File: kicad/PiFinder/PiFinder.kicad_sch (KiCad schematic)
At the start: 24 parts, among them J1 Raspberry_Pi_2_3, J2 display, J3 IMU, SW0 SW_Push_Dual, SW1 SW_Push_Dual, SW2 SW_Push_Dual, SW3 SW_Push_Dual, SW4 SW_Push_Dual, SW5 SW_Push_Dual, SW6 SW_Push_Dual, SW7 SW_Push_Dual, SW8 SW_Push_Dual, SW9 SW_Push_Dual

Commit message: Working capture/solver
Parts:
- J2: symbol Connector:Conn_01x08_Male -> Connector:Conn_01x07_Male
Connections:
- net DISP_CLK: now also J2.4 (Pin_4); no longer J2.5 (Pin_5)
- net DISP_CS: now also J2.5 (Pin_5); no longer J2.6 (Pin_6)
- net DISP_DC: now also J2.6 (Pin_6); no longer J2.7 (Pin_7)
- net DISP_DIN: now also J2.3 (Pin_3); no longer J2.4 (Pin_4)
- net DISP_RST: now also J2.7 (Pin_7); no longer J2.8 (Pin_8)
- no-connect marks 3 -> 2
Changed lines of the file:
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@@
   (junction (at 46.99 180.34) (diameter 0) (color 0 0 0 0)
   )
-  (no_connect (at 45.72 43.18))
   (no_connect (at 99.06 53.34))
   (no_connect (at 99.06 43.18))
@@
     )
   )
-  (global_label "DISP_DC" (shape input) (at 45.72 53.34 0) (fields_autoplaced)
-    (effects (font (size 1.27 1.27)) (justify left))
-    (property "Intersheet References" "${INTERSHEET_REFS}" (id 0) (at 55.9061 53.2606 0)
+  (global_label "DISP_DC" (shape input) (at 45.72 50.8 0) (fields_autoplaced)
+    (effects (font (size 1.27 1.27)) (justify left))
+    (property "Intersheet References" "${INTERSHEET_REFS}" (id 0) (at 55.9061 50.7206 0)
       (effects (font (size 1.27 1.27)) (justify left) hide)
     )
@@
     )
   )
-  (global_label "DISP_RST" (shape input) (at 45.72 55.88 0) (fields_autoplaced)
-    (effects (font (size 1.27 1.27)) (justify left))
-    (property "Intersheet References" "${INTERSHEET_REFS}" (id 0) (at 56.8132 55.8006 0)
-      (effects (font (size 1.27 1.27)) (justify left) hide)
-    )
-  )
-  (global_label "DISP_CLK" (shape input) (at 45.72 48.26 0) (fields_autoplaced)
-    (effects (font (size 1.27 1.27)) (justify left))
-    (property "Intersheet References" "${INTERSHEET_REFS}" (id 0) (at 56.9342 48.1806 0)
-      (effects (font (size 1.27 1.27)) (justify left) hide)
-    )
-  )
-  (global_label "DISP_CS" (shape input) (at 45.72 50.8 0) (fields_autoplaced)
-    (effects (font (size 1.27 1.27)) (justify left))
-    (property "Intersheet References" "${INTERSHEET_REFS}" (id 0) (at 55.8456 50.7206 0)
+  (global_label "DISP_RST" (shape input) (at 45.72 53.34 0) (fields_autoplaced)
+    (effects (font (size 1.27 1.27)) (justify left))
+    (property "Intersheet References" "${INTERSHEET_REFS}" (id 0) (at 56.8132 53.2606 0)
+      (effects (font (size 1.27 1.27)) (justify left) hide)
+    )
+  )
+  (global_label "DISP_CLK" (shape input) (at 45.72 45.72 0) (fields_autoplaced)
+    (effects (font (size 1.27 1.27)) (justify left))
+    (property "Intersheet References" "${INTERSHEET_REFS}" (id 0) (at 56.9342 45.6406 0)
+      (effects (font (size 1.27 1.27)) (justify left) hide)
+    )
+  )
+  (global_label "DISP_CS" (shape input) (at 45.72 48.26 0) (fields_autoplaced)
+    (effects (font (size 1.27 1.27)) (justify left))
+    (property "Intersheet References" "${INTERSHEET_REFS}" (id 0) (at 55.8456 48.1806 0)
       (effects (font (size 1.27 1.27)) (justify left) hide)
     )
@@
     )
   )
-  (global_label "DISP_DIN" (shape input) (at 45.72 45.72 0) (fields_autoplaced)
-    (effects (font (size 1.27 1.27)) (justify left))
-    (property "Intersheet References" "${INTERSHEET_REFS}" (id 0) (at 56.5713 45.6406 0)
+  (global_label "DISP_DIN" (shape input) (at 45.72 43.18 0) (fields_autoplaced)
+    (effects (font (size 1.27 1.27)) (justify left))
+    (property "Intersheet References" "${INTERSHEET_REFS}" (id 0) (at 56.5713 43.1006 0)
       (effects (font (size 1.27 1.27)) (justify left) hide)
     )
@@
     (pin "1")
   )
-  (symbol (lib_id "Connector:Conn_01x08_Male") (at 40.64 45.72 0) (unit 1)
+  (symbol (lib_id "Connector:Conn_01x07_Male") (at 40.64 45.72 0) (unit 1)
     (in_bom yes) (on_board yes) (fields_autoplaced)
     (property "Reference" "J2" (id 0) (at 41.275 34.324 0))
@@
     (pin "6")
     (pin "7")
-    (pin "8")
   )
   (symbol (lib_id "power:GND") (at 59.69 40.64 0) (unit 1)

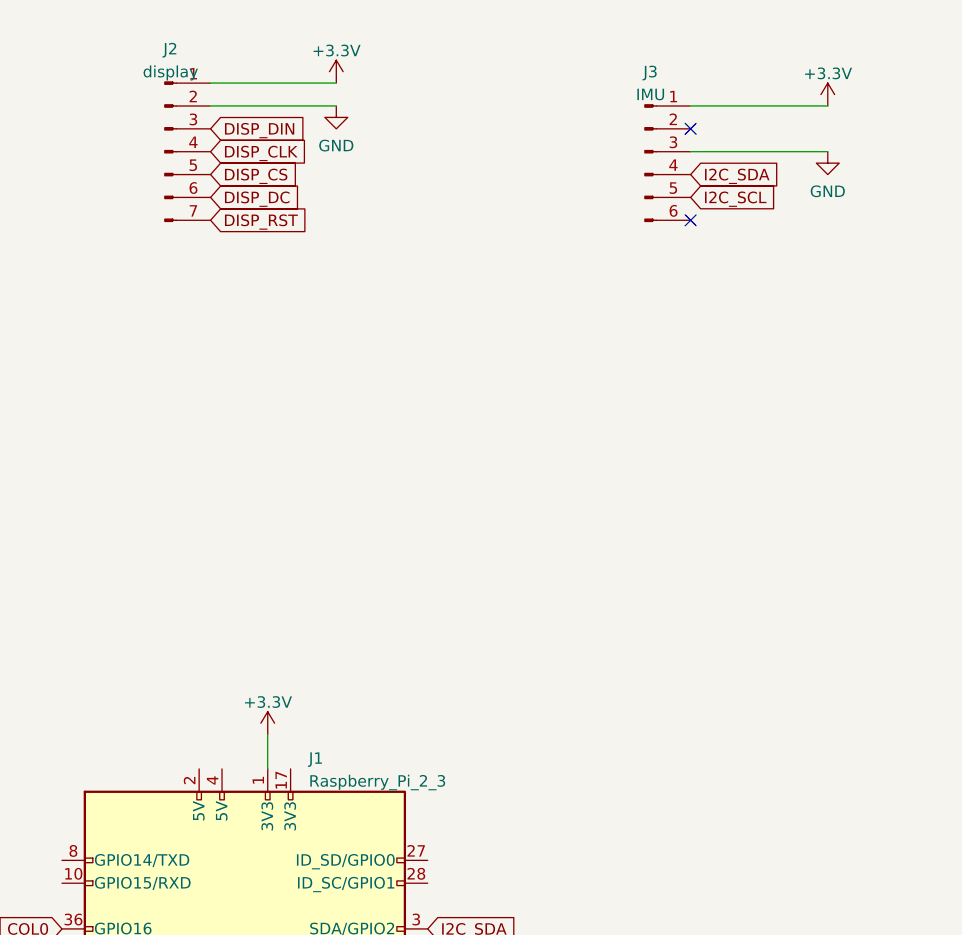
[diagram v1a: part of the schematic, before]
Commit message: Add power, fix imu connection to main PCB
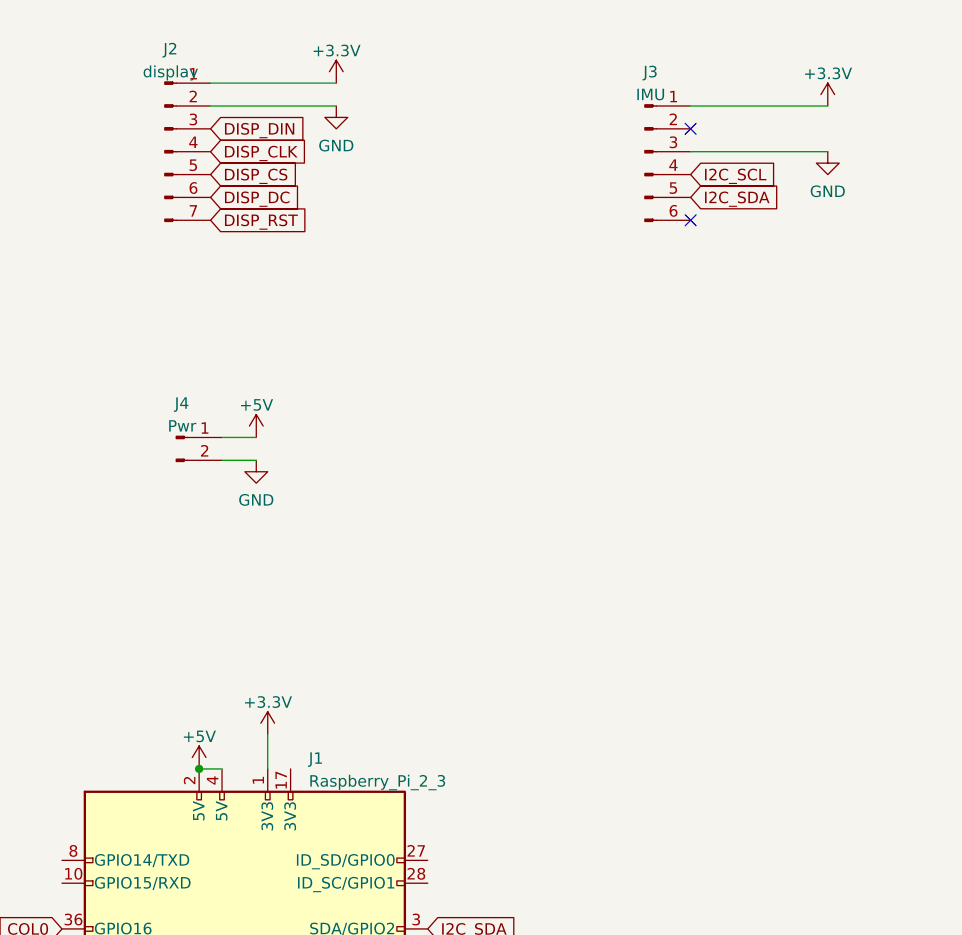
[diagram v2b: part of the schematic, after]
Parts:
- added J4: Pwr, Connector_PinHeader_2.00mm:PinHeader_1x02_P2.00mm_Horizontal, symbol Connector:Conn_01x02_Male
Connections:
- net GND: now also J4.2 (Pin_2)
- net I2C_SCL: now also J3.4 (Pin_4); no longer J3.5 (Pin_5)
- net I2C_SDA: now also J3.5 (Pin_5); no longer J3.4 (Pin_4)
- net +5V: now reaches J1.2 (5V)
- net +5V: now also J1.4 (5V), J4.1 (Pin_1)
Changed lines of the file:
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@@
   (junction (at 218.44 128.27) (diameter 0) (color 0 0 0 0)
+  )
+  (junction (at 44.45 114.3) (diameter 0) (color 0 0 0 0)
   )
   (junction (at 217.17 36.83) (diameter 0) (color 0 0 0 0)
@@
     (stroke (width 0) (type default) (color 0 0 0 0))
   )
+  (wire (pts (xy 44.45 114.3) (xy 46.99 114.3))
+    (stroke (width 0) (type default) (color 0 0 0 0))
+  )
   (wire (pts (xy 218.44 97.79) (xy 218.44 107.95))
     (stroke (width 0) (type default) (color 0 0 0 0))
@@
     (stroke (width 0) (type default) (color 0 0 0 0))
   )
+  (wire (pts (xy 46.99 80.01) (xy 50.8 80.01))
+    (stroke (width 0) (type default) (color 0 0 0 0))
+  )
   (wire (pts (xy 264.16 123.19) (xy 262.89 123.19))
     (stroke (width 0) (type default) (color 0 0 0 0))
@@
     (stroke (width 0) (type default) (color 0 0 0 0))
   )
+  (wire (pts (xy 46.99 77.47) (xy 50.8 77.47))
+    (stroke (width 0) (type default) (color 0 0 0 0))
+  )
   (wire (pts (xy 218.44 128.27) (xy 241.3 128.27))
     (stroke (width 0) (type default) (color 0 0 0 0))
@@
     )
   )
-  (global_label "I2C_SDA" (shape input) (at 99.06 48.26 0) (fields_autoplaced)
-    (effects (font (size 1.27 1.27)) (justify left))
-    (property "Intersheet References" "${INTERSHEET_REFS}" (id 0) (at 109.0042 48.1806 0)
+  (global_label "I2C_SDA" (shape input) (at 99.06 50.8 0) (fields_autoplaced)
+    (effects (font (size 1.27 1.27)) (justify left))
+    (property "Intersheet References" "${INTERSHEET_REFS}" (id 0) (at 109.0042 50.7206 0)
       (effects (font (size 1.27 1.27)) (justify left) hide)
     )
@@
     )
   )
-  (global_label "I2C_SCL" (shape input) (at 99.06 50.8 0) (fields_autoplaced)
-    (effects (font (size 1.27 1.27)) (justify left))
-    (property "Intersheet References" "${INTERSHEET_REFS}" (id 0) (at 108.9437 50.7206 0)
+  (global_label "I2C_SCL" (shape input) (at 99.06 48.26 0) (fields_autoplaced)
+    (effects (font (size 1.27 1.27)) (justify left))
+    (property "Intersheet References" "${INTERSHEET_REFS}" (id 0) (at 108.9437 48.1806 0)
       (effects (font (size 1.27 1.27)) (justify left) hide)
     )
@@
     )
     (property "Datasheet" "~" (id 3) (at 256.54 96.52 0)
+      (effects (font (size 1.27 1.27)) hide)
+    )
+    (pin "1")
+    (pin "2")
+  )
+  (symbol (lib_id "Connector:Conn_01x02_Male") (at 41.91 77.47 0) (unit 1)
+    (in_bom yes) (on_board yes) (fields_autoplaced)
+    (property "Reference" "J4" (id 0) (at 42.545 73.694 0))
+    (property "Value" "Pwr" (id 1) (at 42.545 76.2309 0))
+    (property "Footprint" "Connector_PinHeader_2.00mm:PinHeader_1x02_P2.00mm_Horizontal" (id 2) (at 41.91 77.47 0)
+      (effects (font (size 1.27 1.27)) hide)
+    )
+    (property "Datasheet" "~" (id 3) (at 41.91 77.47 0)
       (effects (font (size 1.27 1.27)) hide)
     )
@@
     (pin "1")
     (pin "2")
+  )
+  (symbol (lib_id "power:+5V") (at 44.45 114.3 0) (unit 1)
+    (in_bom yes) (on_board yes) (fields_autoplaced)
+    (property "Reference" "#PWR0108" (id 0) (at 44.45 118.11 0)
+      (effects (font (size 1.27 1.27)) hide)
+    )
+    (property "Value" "+5V" (id 1) (at 44.45 110.7242 0))
+    (property "Footprint" "" (id 2) (at 44.45 114.3 0)
+      (effects (font (size 1.27 1.27)) hide)
+    )
+    (property "Datasheet" "" (id 3) (at 44.45 114.3 0)
+      (effects (font (size 1.27 1.27)) hide)
+    )
+    (pin "1")
   )
   (symbol (lib_id "power:+3.3V") (at 114.3 40.64 0) (unit 1)
@@
     (pin "7")
   )
+  (symbol (lib_id "power:+5V") (at 50.8 77.47 0) (unit 1)
+    (in_bom yes) (on_board yes) (fields_autoplaced)
+    (property "Reference" "#PWR0109" (id 0) (at 50.8 81.28 0)
+      (effects (font (size 1.27 1.27)) hide)
+    )
+    (property "Value" "+5V" (id 1) (at 50.8 73.8942 0))
+    (property "Footprint" "" (id 2) (at 50.8 77.47 0)
+      (effects (font (size 1.27 1.27)) hide)
+    )
+    (property "Datasheet" "" (id 3) (at 50.8 77.47 0)
+      (effects (font (size 1.27 1.27)) hide)
+    )
+    (pin "1")
+  )
   (symbol (lib_id "power:GND") (at 59.69 40.64 0) (unit 1)
     (in_bom yes) (on_board yes) (fields_autoplaced)
@@
     )
     (property "Datasheet" "" (id 3) (at 59.69 40.64 0)
+      (effects (font (size 1.27 1.27)) hide)
+    )
+    (pin "1")
+  )
+  (symbol (lib_id "power:GND") (at 50.8 80.01 0) (unit 1)
+    (in_bom yes) (on_board yes) (fields_autoplaced)
+    (property "Reference" "#PWR0107" (id 0) (at 50.8 86.36 0)
+      (effects (font (size 1.27 1.27)) hide)
+    )
+    (property "Value" "GND" (id 1) (at 50.8 84.4534 0))
+    (property "Footprint" "" (id 2) (at 50.8 80.01 0)
+      (effects (font (size 1.27 1.27)) hide)
+    )
+    (property "Datasheet" "" (id 3) (at 50.8 80.01 0)
       (effects (font (size 1.27 1.27)) hide)
     )
@@
       (reference "#PWR0106") (unit 1) (value "+3.3V") (footprint "")
     )
+    (path "/dcd97a4b-6c14-42a8-b5f8-43f2805bcbdb"
+      (reference "#PWR0107") (unit 1) (value "GND") (footprint "")
+    )
+    (path "/7eab7327-8e7d-4f71-a45d-d0dd3546a0a1"
+      (reference "#PWR0108") (unit 1) (value "+5V") (footprint "")
+    )
+    (path "/bb557f14-cc55-4402-b970-d3069ded7cf5"
+      (reference "#PWR0109") (unit 1) (value "+5V") (footprint "")
+    )
     (path "/00000000-0000-0000-0000-000062b179fc"
       (reference "H1") (unit 1) (value "Hole_Pad") (footprint "Horizon:Mount_M2.5")
@@
       (reference "J3") (unit 1) (value "IMU") (footprint "RSU:Adafruit_BNO055_IMU")
     )
+    (path "/0a895e67-511e-4a33-8111-57bf512943f6"
+      (reference "J4") (unit 1) (value "Pwr") (footprint "Connector_PinHeader_2.00mm:PinHeader_1x02_P2.00mm_Horizontal")
+    )
     (path "/00000000-0000-0000-0000-000062b6f7a2"

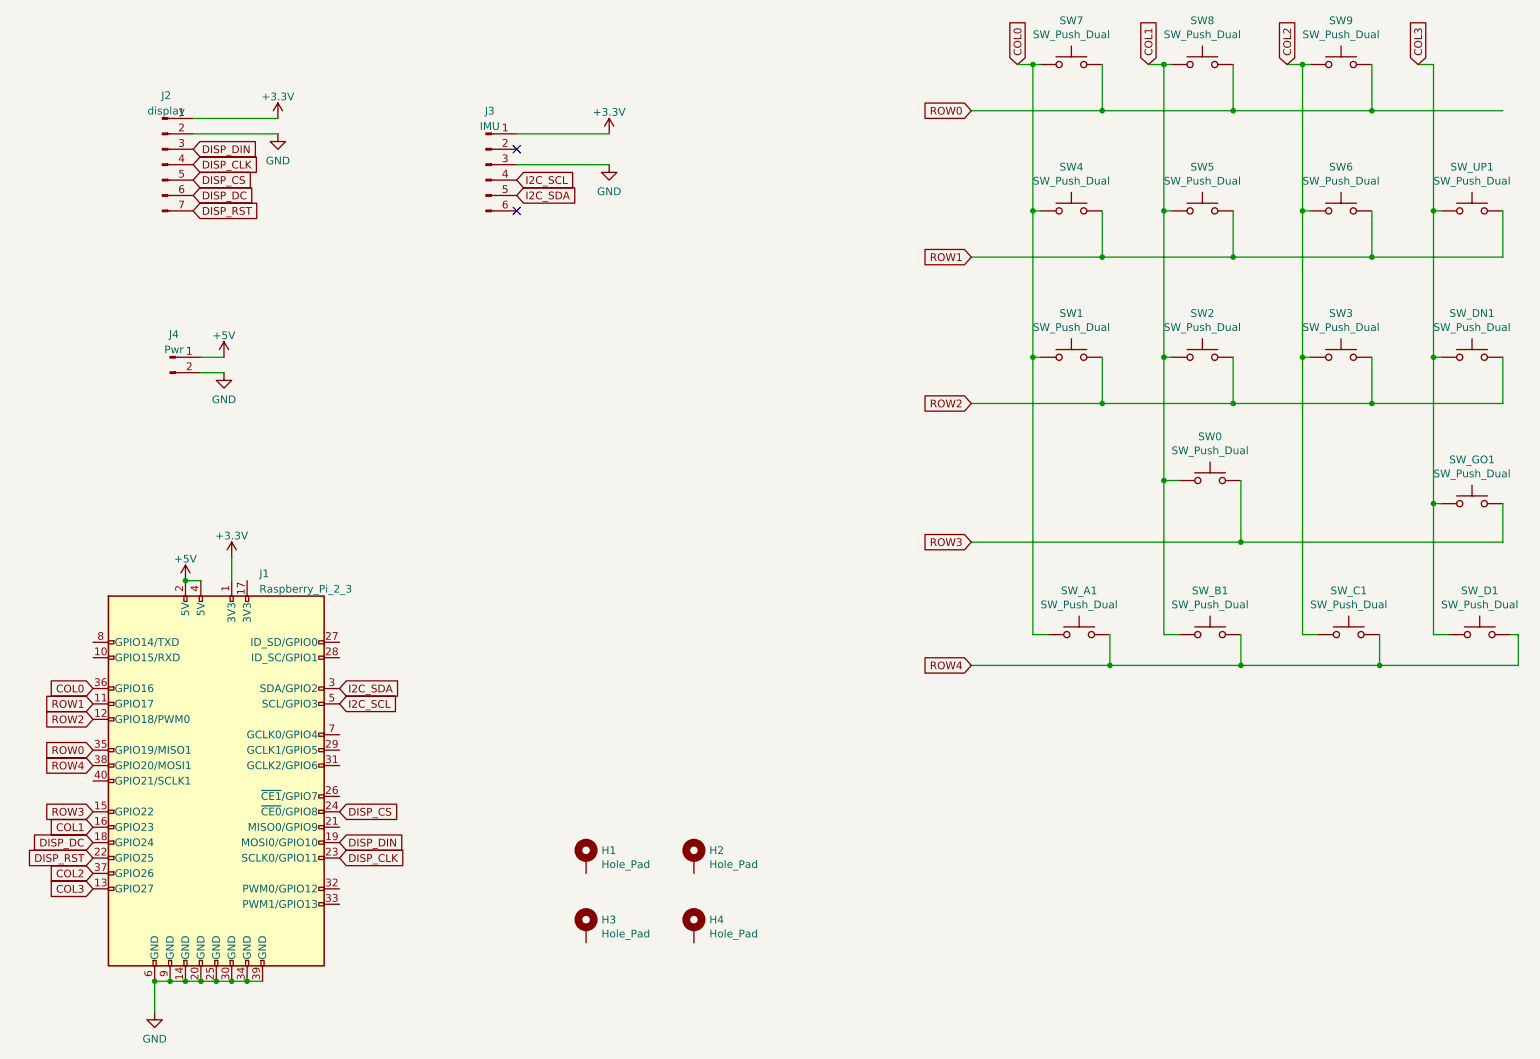
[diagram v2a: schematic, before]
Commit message: New PCB with backlight
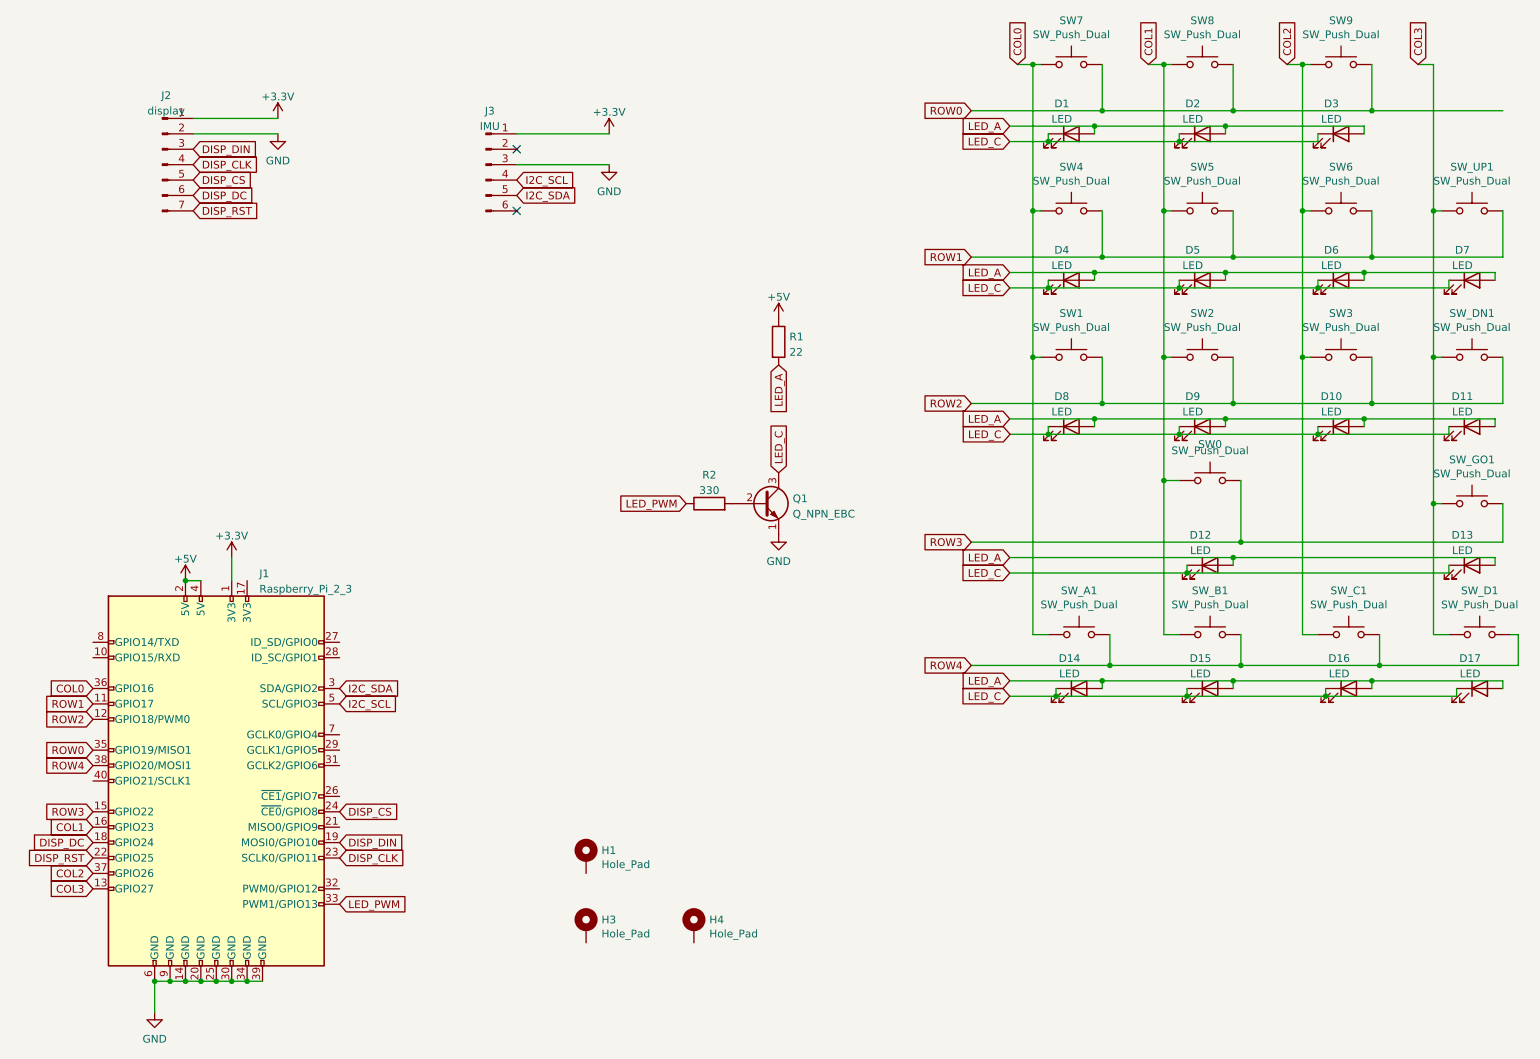
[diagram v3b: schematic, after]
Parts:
- removed H2: Hole_Pad, Horizon:Mount_M2.5, symbol handipi_kb-rescue:Hole_Pad-horizon
- removed J4: Pwr, Connector_PinHeader_2.00mm:PinHeader_1x02_P2.00mm_Horizontal, symbol Connector:Conn_01x02_Male
- added D1, D10, D11, D12, D13, D14, D15, D16, D17, D2, D3, D4, D5, D6, D7, D8, D9: LED, LED_THT:LED_D1.8mm_W3.3mm_H2.4mm, symbol Device:LED
- added Q1: Q_NPN_EBC, Package_TO_SOT_THT:TO-92_Inline_Wide, symbol Device:Q_NPN_EBC
- added R1: 22, Resistor_THT:R_Axial_DIN0207_L6.3mm_D2.5mm_P10.16mm_Horizontal, symbol Device:R
- added R2: 330, Resistor_THT:R_Axial_DIN0207_L6.3mm_D2.5mm_P10.16mm_Horizontal, symbol Device:R
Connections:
- net +5V: now also R1.1
- net GND: now also Q1.1 (E)
- net LED_PWM: now reaches J1.33 (PWM1/GPIO13)
- net LED_PWM: now also R2.1
- new net: Q1.2 (B), R2.2
- new net LED_A: D1.2 (A), D10.2 (A), D11.2 (A), D12.2 (A), D13.2 (A), D14.2 (A), D15.2 (A), D16.2 (A), D17.2 (A), D2.2 (A), D3.2 (A), D4.2 (A), D5.2 (A), D6.2 (A), D7.2 (A), D8.2 (A), D9.2 (A), R1.2
- new net LED_C: D1.1 (K), D10.1 (K), D11.1 (K), D12.1 (K), D13.1 (K), D14.1 (K), D15.1 (K), D16.1 (K), D17.1 (K), D2.1 (K), D3.1 (K), D4.1 (K), D5.1 (K), D6.1 (K), D7.1 (K), D8.1 (K), D9.1 (K), Q1.3 (C)
